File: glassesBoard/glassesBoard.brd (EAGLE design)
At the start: 82.9 x 28.4 mm, 90 parts, among them J1 BM10NB(0.8)-16DS-0.4V(51), J2 DF30FC-30DS-0.4V, J3 S2B-XH-A(LF)(SN), J7 105450-0101, U10 ATTINY20-MMH, U11 SN65LVDS822VQFN48, U12 NLAS2750, U13 NX3020NAK, U14 SSM3J338RSOT-23F, U15 NX3020NAK, U16 SSM3J338RSOT-23F, U17 NX3020NAK, U18 2.8, U19 TCR2EF15SOT-25, U2 TPS613222A, U20 MICROSD, U21 MCP73833, U3 1.8, U4 3.3, U5 SSM3J338RSOT-23F, U6 SSM3J338RSOT-23F, U7 SN65DSI83PBGA-N64, U8 IQS263BDFN10, U9 NX3020NAK

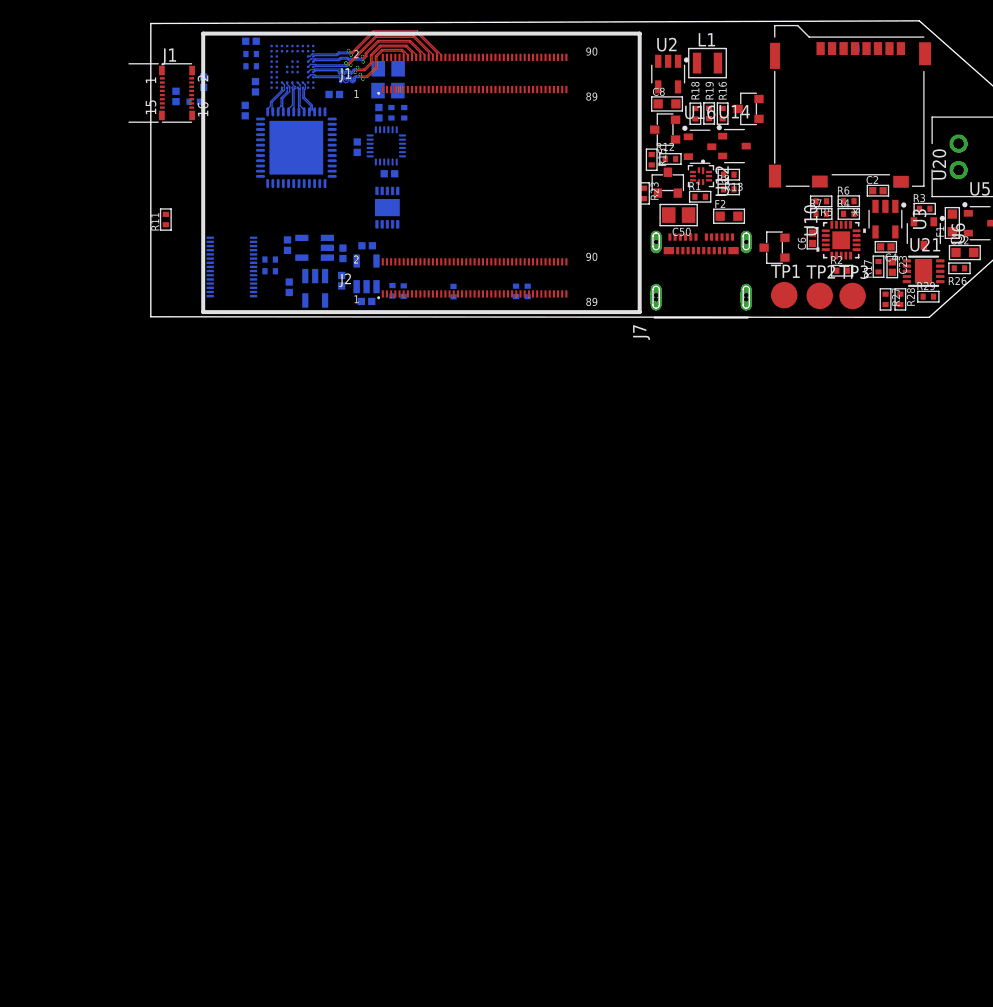
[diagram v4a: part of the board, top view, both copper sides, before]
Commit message: Added gesture board, more level shifting and light sensor
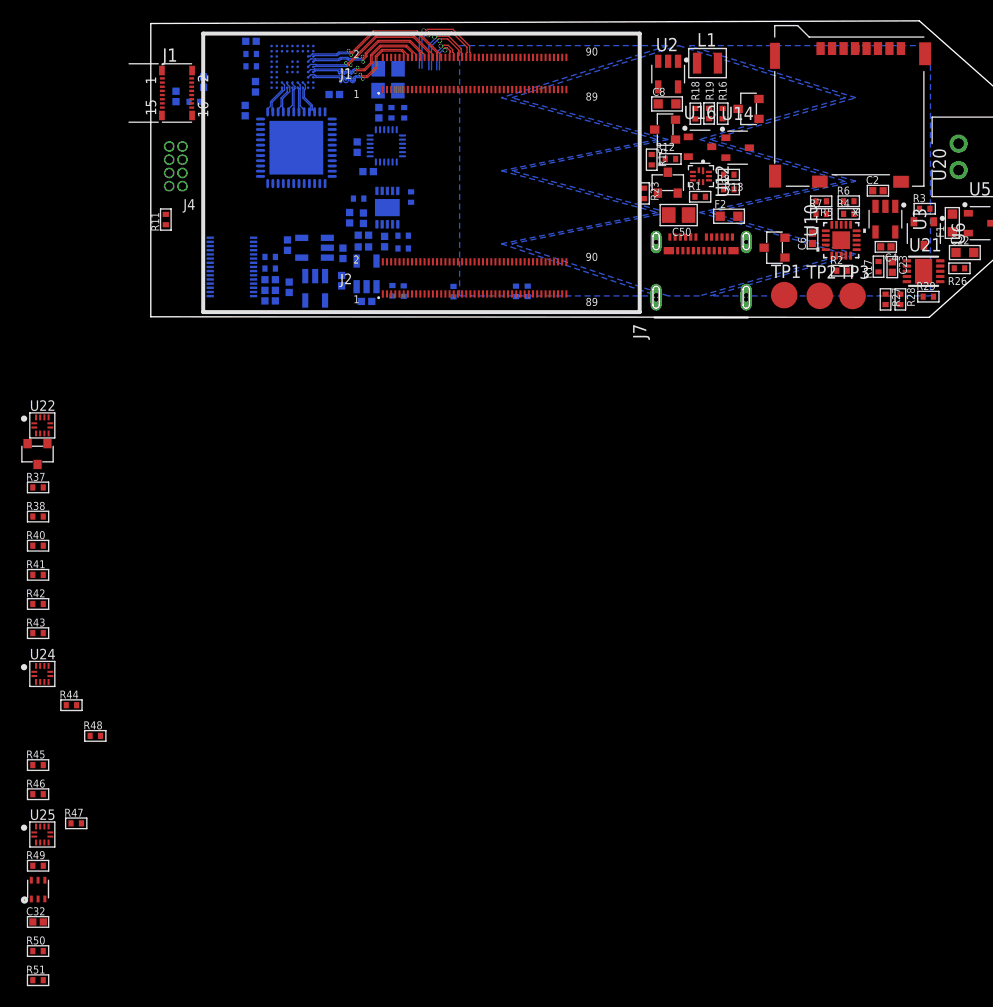
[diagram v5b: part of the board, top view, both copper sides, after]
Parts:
- added C25, C27, C29, C30, C31: 1uF, thanics-capacitor:C0402
- added C26, C28, C32: 100nF, thanics-capacitor:C0402
- added J4: GRPB042MWCN-RC, thanics-connector:GRPB042MWCN-RC
- added R34, R35, R36: 470R, thanics-resistor:R0402
- added R37, R41, R42, R43, R44, R45, R46, R47, R48, R49, R50, R51: 10k, thanics-resistor:R0402
- added R38, R39, R40: 5.1k, thanics-resistor:R0402
- added U22, U24, U25: FXMA2104UMX, glasses:12MLP
- added U23: NX3020NAK, glasses:SOT-23_(TO-236AB)
- added U26: LTR-303ALS-01, glasses:LTR-303ALS-01
- moved C20 2.06 mm to (25.1, 13.9), turned to 0 degrees
- moved C5 0.37 mm to (24.6, 6.71)
- moved U14 0.34 mm to (60.5, 16.2)
- moved R31 0.25 mm to (15.7, 5.74)
- moved R30 0.25 mm to (15.7, 4.62)
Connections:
- removed net !RST: R2.2, TP3.TP, U10.13
- removed net !SHUTDOWN_INT: U10.2
- removed net I2C_SCL_5V: U10.15
- removed net I2C_SDA_5V/TPIDATA: TP2.TP, U10.12
- new net !FINGER_INT_1V8: R48.1, U24.12
- new net !FINGER_INT_5V: R46.1, U10.14, U24.3
- new net !GESTURE_INT: R49.1, U$1.J2.52, U25.10
- new net !GESTURE_INT_3V3: J4.7, U25.5
- new net !LIGHT_INT: R50.1, U$1.J2.54, U25.9
- new net !LIGHT_INT_3V3: R51.1, U25.6, U26.5
- new net !SHUTDOWN_INT_1V8: R43.1, U22.9
- new net !SHUTDOWN_INT_5V: R41.1, U10.2, U22.6
- new net !TOUCH_INT_1V8: U24.11
- new net !TOUCH_INT_5V: R45.1, U10.17, U24.4
- new net !TPI_RST_1V8: R42.1, U22.12
- new net !TPI_RST_5V: R2.2, TP3.TP, U10.13, U22.3
- new net EXT_PROG_EN: U$1.J2.14, U23.G
- new net I2C0_SCL_3V3: J4.2, U25.4, U26.4
- new net I2C0_SCL_5V: R40.1, U10.15, U22.4
- new net I2C0_SDA_3V3: J4.8, U25.3, U26.6
- new net I2C0_SDA_5V/TPIDATA: R38.1, TP2.TP, U10.12, U22.5
- new net LED_B: J4.4, U$1.J2.60
- new net LED_G: J4.3, U$1.J2.58
- new net LED_R: J4.5, U$1.J2.6
- new net N$30: R36.1, U8.9
- new net N$31: R35.1, U8.3
- new net N$32: R34.1, U8.2
- new net N$33: R37.1, U22.8, U23.D
- new net N$35: R44.1, U24.8
- new net N$36: R47.1, U25.8
- new net N$37: C27.1, C28.1, U8.5
- new net RX1: R34.2
- new net RX2: R35.2
- new net RX3: R36.2
- net !TOUCH_INT: now also R39.1, U$1.J2.12
- net +1V5: now also C30.1
- net +1V8: now also C25.1, C26.1, C29.1, R39.2, R42.2, R43.2, R48.2, R49.2, R50.2, U11.17, U11.43, U11.6, U22.1, U24.1, U25.1, U8.4
- net +2V8: now also C31.1
- net +3V3: now also C32.1, J4.1, R47.2, R51.2, U25.2, U26.1; no longer U8.4
- net +5V: now also R37.2, R38.2, R40.2, R41.2, R44.2, R45.2, R46.2, U22.2, U24.2
- net DSI_EN: now also U$1.J2.63
- net GND: now also C25.2, C26.2, C27.2, C28.2, C29.2, C30.2, C31.2, C32.2, J4.6, U22.7, U23.S, U24.7, U25.7, U26.3, U8.1, U8.EXP
- net I2C0_SCL: now also U22.11, U25.11, U8.8
- net I2C0_SDA: now also U22.10, U25.12, U8.7
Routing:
- net MIPI_CSI1_DATA0_P: track 0.00 -> 10.2 mm, vias 0 -> 1
- net MIPI_CSI1_DATA0_N: track 0.00 -> 9.37 mm, vias 0 -> 1
- net MIPI_CSI1_DATA1_P: track 0.00 -> 7.53 mm, vias 0 -> 1
- net MIPI_CSI1_DATA1_N: track 0.00 -> 6.75 mm, vias 0 -> 1
- net MIPI_CSI1_CLK_P: track 0.00 -> 4.77 mm, vias 0 -> 1
- net MIPI_CSI1_CLK_N: track 0.00 -> 3.91 mm, vias 0 -> 1
- added copper zone on layer 16, net RX1
- added copper zone on layer 16, net RX2
- added copper zone on layer 16, net RX3

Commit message: Layout almost done
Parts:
- removed C16, C17, C21, C24: 1uF, thanics-capacitor:C0402
- removed R14, R25: 10k, thanics-resistor:R0402
- removed U11: SN65LVDS822VQFN48, glasses:QFN50P700X700X100-49T515
- removed U7: SN65DSI83PBGA-N64, glasses:BGA81C50P9X9_500X500X100
- added J10, J11, J5, J6, J8, J9: U.FL, thanics-connector:U.FL
- added R52: 10k, thanics-resistor:R0402
- moved R46 95.1 mm to (70.0, 10.7), turned to 90 degrees
- moved R45 92.4 mm to (68.6, 10.7), turned to 90 degrees
- moved R44 85.2 mm to (66.3, 11.8)
- moved U24 85.1 mm to (66.6, 9.86), turned to 90 degrees
- moved R41 82.6 mm to (69.2, 8.13)
- moved R48 81.8 mm to (64.1, 9.19), turned to 180 degrees
- moved R40 80.4 mm to (68.9, 5.69)
- moved R43 80.2 mm to (63.9, 7.95), turned to 180 degrees
- moved R38 80.1 mm to (69.2, 6.91)
- moved R42 77.9 mm to (63.8, 6.05), turned to 180 degrees
- moved R37 76.9 mm to (66.4, 7.95)
- moved R50 76.4 mm to (11.8, 13.3), flipped to the bottom, turned to 90 degrees
- moved R51 74.4 mm to (10.3, 8.84), flipped to the bottom, turned to 180 degrees
- moved U22 74.1 mm to (66.1, 6.10), turned to 90 degrees
- moved U23 72.6 mm to (64.1, 2.97), turned to 180 degrees
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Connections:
- removed net !SHUTDOWN_LVDS: U11.37
- removed net FINGER_INT: J1.8, U$1.J1.73
- removed net N$1: U11.26, U7.C8
- removed net N$10: U11.33, U7.G9
- removed net N$11: U11.32, U7.F8
- removed net N$12: U11.31, U7.F9
- removed net N$15: C16.1, U7.J8
- removed net N$26: R14.2, U7.A1, U7.H2
- removed net N$3: U11.25, U7.C9
- removed net N$4: U11.28, U7.D8
- removed net N$5: U11.27, U7.D9
- removed net N$7: U11.30, U7.E8
- removed net N$8: U11.29, U7.E9
- removed net N$9: U11.34, U7.G8
- new net N$34: R52.1
- net !FINGER_INT_1V8: now also J1.8, U$1.J1.73
- net !TOUCH_INT: no longer U$1.J2.12
- net !TOUCH_INT_1V8: now also U$1.J2.12
- net !TOUCH_INT_5V: now also U10.1; no longer U10.17
- net !TPI_RST_1V8: now also U22.11; no longer U22.12
- net !TPI_RST_5V: now also U22.4; no longer U22.3
- net +1V8: now also R52.2; no longer C17.1, R25.1, U11.17, U11.43, U11.6, U7.A9, U7.B8, U7.D6, U7.E5, U7.E6, U7.F6, U7.J2
- net +3V3: no longer C24.1, U11.24, U11.44
- net BATT_CNTL: now also U10.17; no longer U10.1
- net DSI_EN: no longer C21.1, R25.2, U7.B1
- net GND: now also J10.P$1, J10.P$2, J11.P$1, J11.P$2, J5.P$1, J5.P$2, J6.P$1, J6.P$2, J8.P$1, J8.P$2, J9.P$1, J9.P$2; no longer C16.2, C17.2, C21.2, C24.2, R14.1, U11.36, U11.45, U11.49, U7.A2, U7.A8, U7.B9, U7.D5, U7.E4, U7.F4, U7.F5, U7.H9
- net I2C0_SCL: now also U22.12; no longer U22.11
- net I2C0_SCL_5V: now also U22.3; no longer U22.4
- net I2C3_SCL: no longer U7.H1
- net I2C3_SDA: no longer U7.J1
- net LED_B: now also U$1.J2.2
- net LED_G: now also U$1.J2.8
- net MIPI_DSI0_CLK_N: now also J11.P$3; no longer U7.J5
- net MIPI_DSI0_CLK_P: now also J10.P$3; no longer U7.H5
- net MIPI_DSI0_DATA0_N: now also J6.P$3; no longer U7.J3
- net MIPI_DSI0_DATA0_P: now also J5.P$3; no longer U7.H3
- net MIPI_DSI0_DATA1_N: now also J9.P$3; no longer U7.J4
- net MIPI_DSI0_DATA1_P: now also J8.P$3; no longer U7.H4
- net MIPI_DSI0_DATA2_N: no longer U7.J6
- net MIPI_DSI0_DATA2_P: no longer U7.H6
- net MIPI_DSI0_DATA3_N: no longer U7.J7
- net MIPI_DSI0_DATA3_P: no longer U7.H7
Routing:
- net P$1: track 0.00 -> 104.2 mm, vias 0 -> 3
- net I2C0_SCL: track 0.00 -> 70.1 mm, vias 0 -> 6
- net I2C0_SDA: track 0.00 -> 69.6 mm, vias 0 -> 6
- net CHARGER_VCC: track 0.00 -> 62.2 mm, vias 0 -> 3
- net CHARGE_STAT2: track 0.00 -> 57.3 mm, vias 0 -> 2
- net CHARGE_STAT1: track 0.00 -> 57.0 mm, vias 0 -> 2
- net +5V: track 0.00 -> 51.0 mm, vias 0 -> 7
- net USB_HS_ID: track 0.00 -> 48.4 mm, vias 0 -> 6
- net MIPI_CSI1_DATA0_N: track 9.37 -> 54.9 mm, vias 1 -> 3
- net MIPI_CSI1_DATA0_P: track 10.2 -> 55.4 mm, vias 1 -> 3
- net SPI0_MISO: track 0.00 -> 43.1 mm, vias 0 -> 2
- net MIPI_CSI1_CLK_N: track 3.91 -> 44.9 mm, vias 1 -> 3
- net MIPI_CSI1_CLK_P: track 4.77 -> 45.7 mm, vias 1 -> 3
- net SPI0_MOSI: track 0.00 -> 40.6 mm, vias 0 -> 2
- net !FINGER_RST: track 0.00 -> 39.5 mm, vias 0 -> 3
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- added copper zone on layer 2, net +1V8
- added copper zone on layer 1, net GND
- added copper zone on layer 15, net GND
- added copper zone on layer 16, net GND
- removed copper zone on layer 16, net RX1
- removed copper zone on layer 16, net RX2
- removed copper zone on layer 16, net RX3
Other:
- board size 82.9 x 28.4 mm -> 82.9 x 29.2 mm

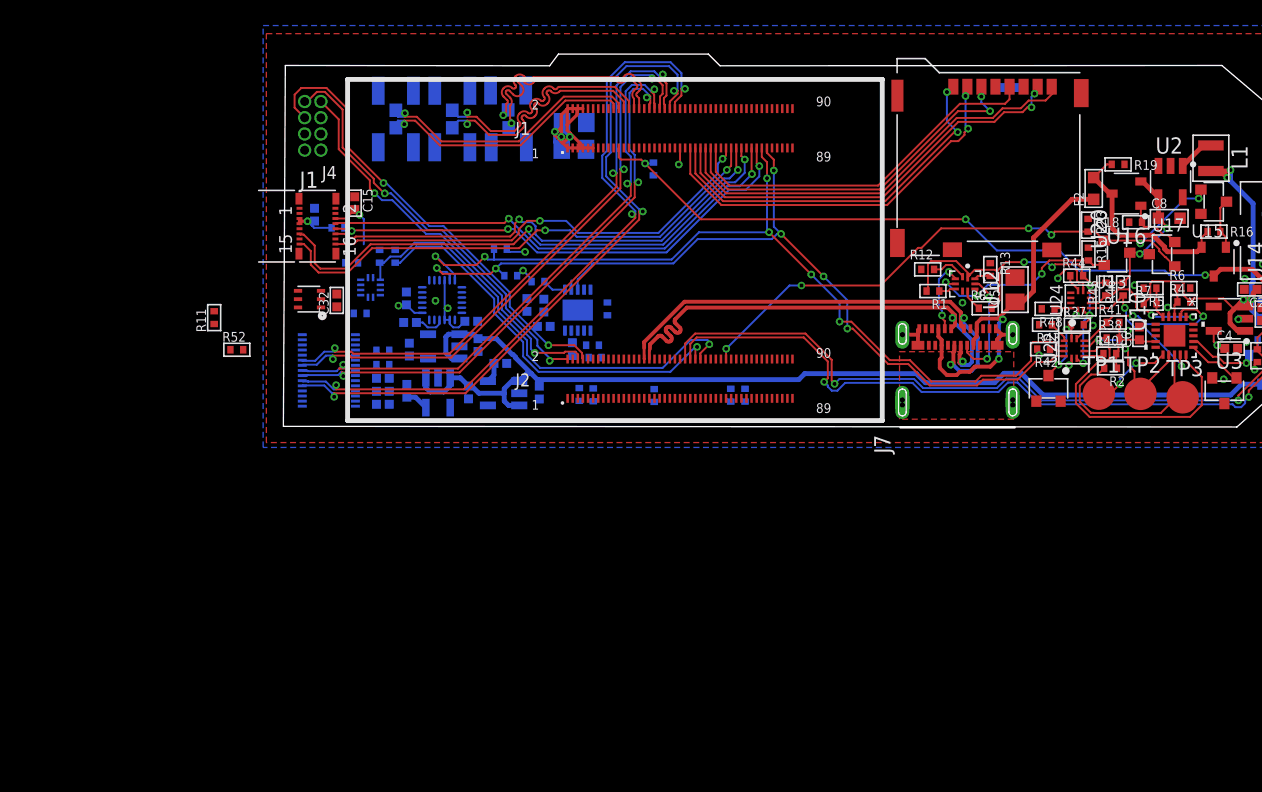
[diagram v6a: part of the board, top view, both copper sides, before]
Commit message: Removed light sensor, added serial port pins, added touch panel connector, small schematic fixes
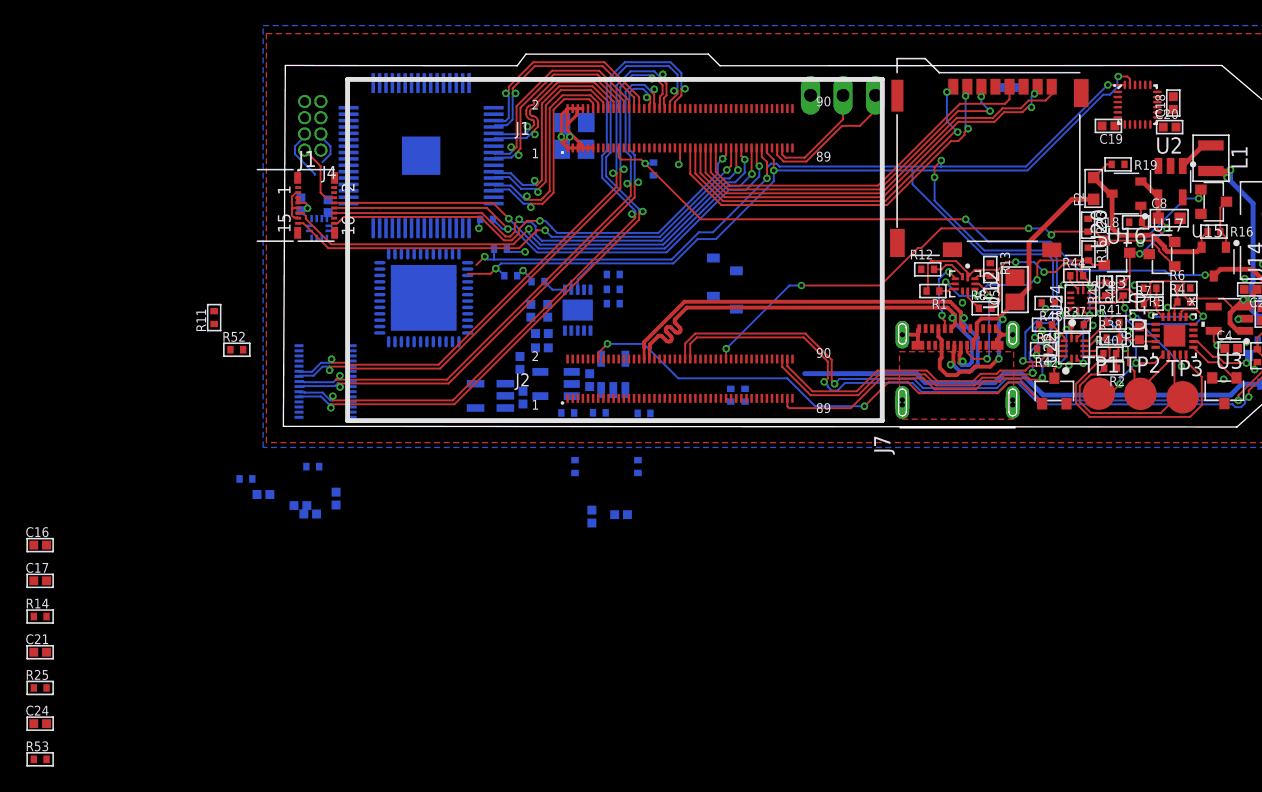
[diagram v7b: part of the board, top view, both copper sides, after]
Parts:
- removed C32: 100nF, thanics-capacitor:C0402
- removed J10, J11, J6, J8, J9: U.FL, thanics-connector:U.FL
- removed R50, R51: 10k, thanics-resistor:R0402
- removed U26: LTR-303ALS-01, glasses:LTR-303ALS-01
- added C16, C17, C21, C24: 1uF, thanics-capacitor:C0402
- added JP1: (no value), pinhead:1X03/90
- added R14, R25, R53: 10k, thanics-resistor:R0402
- added U11: SN65LVDS822VQFN48, glasses:QFN50P700X700X100-49T515
- added U7: SN65DSI83-Q1S-PQFP-G64, glasses:QFP50P1200X1200X120-65T300
- J5: value U.FL -> 0787324001; device thanics-connector:U.FL -> thanics-connector:0787324001
- moved C18 61.9 mm to (73.9, 25.3), flipped to the top
- moved C20 61.4 mm to (73.6, 23.4), flipped to the top
- moved U1 56.5 mm to (71.1, 25.2), flipped to the top
- moved C19 52.2 mm to (68.8, 23.5), flipped to the top
- moved R49 25.1 mm to (32.0, -3.15)
- moved R47 23.7 mm to (27.1, -3.15), turned to 90 degrees
- moved J5 22.7 mm to (38.8, 11.2), turned to 90 degrees
- moved C5 15.1 mm to (30.7, -6.91)
- moved R31 14.7 mm to (1.32, -4.11)
- moved C29 13.0 mm to (2.69, -5.33)
- moved R20 11.7 mm to (20.2, 16.2)
- moved C30 11.0 mm to (5.59, -6.20)
- moved C3 10.5 mm to (28.4, -7.06)
- moved C31 10.3 mm to (6.35, -6.86)
- moved C13 10.1 mm to (8.38, -5.65)
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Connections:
- removed net !LIGHT_INT: R50.1, U$1.J2.54, U25.9
- removed net !LIGHT_INT_3V3: R51.1, U25.6, U26.5
- new net !SHUTDOWN_LVDS: U11.37
- new net N$1: U11.26, U7.46
- new net N$10: U11.33, U7.37
- new net N$11: U11.32, U7.38
- new net N$12: U11.31, U7.39
- new net N$15: R53.2, U7.17
- new net N$26: C17.1, U7.31
- new net N$3: U11.25, U7.47
- new net N$39: R25.2, U7.64
- new net N$4: U11.28, U7.44
- new net N$5: U11.27, U7.45
- new net N$7: U11.30, U7.41
- new net N$8: U11.29, U7.42
- new net N$9: U11.34, U7.36
- new net TPICLK_1V8: U$1.J2.87, U24.12
- new net UART1_RX: JP1.2, U$1.J1.85
- new net UART1_TX: JP1.1, U$1.J1.83
- net !FINGER_INT_1V8: now also U24.11; no longer U24.12
- net !FINGER_INT_5V: now also U24.4; no longer U24.3
- net !SHUTDOWN_INT_1V8: now also U$1.J2.88
- net !TOUCH_INT_1V8: now also U24.10; no longer U24.11
- net !TOUCH_INT_5V: now also U24.5; no longer U24.4
- net !TPI_RST_1V8: now also U$1.J2.86
- net +1V8: now also C16.1, R14.1, U11.17, U11.43, U11.6, U7.14, U7.18, U7.3, U7.32, U7.35, U7.40, U7.43, U7.48, U7.49, U7.55, U7.58, U7.63; no longer R50.2
- net +3V3: now also C24.1, U11.24, U11.44; no longer C32.1, R51.2, U26.1
- net DSI_EN: now also C21.1, R14.2, U7.2
- net GND: now also C16.2, C17.2, C21.2, C24.2, J5.4, JP1.3, R25.1, R53.1, U11.36, U11.45, U11.49, U7.23, U7.26, U7.52, U7.65; no longer C32.2, J10.P$1, J10.P$2, J11.P$1, J11.P$2, J5.P$1, J5.P$2, J6.P$1, J6.P$2, J8.P$1, J8.P$2, J9.P$1, J9.P$2, U26.3
- net I2C0_SCL_3V3: no longer U26.4
- net I2C0_SDA_3V3: no longer U26.6
- net I2C3_SCL: now also U7.15
- net I2C3_SDA: now also U7.16
- net MIPI_DSI0_CLK_N: now also U7.25; no longer J11.P$3
- net MIPI_DSI0_CLK_P: now also U7.24; no longer J10.P$3
- net MIPI_DSI0_DATA0_N: now also U7.20; no longer J6.P$3
- net MIPI_DSI0_DATA0_P: now also U7.19; no longer J5.P$3
- net MIPI_DSI0_DATA1_N: now also U7.22; no longer J9.P$3
- net MIPI_DSI0_DATA1_P: now also U7.21; no longer J8.P$3
- net MIPI_DSI0_DATA2_N: now also U7.28
- net MIPI_DSI0_DATA2_P: now also U7.27
- net MIPI_DSI0_DATA3_N: now also U7.30
- net MIPI_DSI0_DATA3_P: now also U7.29
- net RX1: now also J5.2
- net RX2: now also J5.1
- net RX3: now also J5.3
- net TPICLK: now also U24.3
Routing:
- net P$1: track 104.2 -> 54.5 mm, vias 3 -> 2
- net EXT_PROG_EN: track 0.00 -> 39.7 mm, vias 0 -> 2
- net LED_G: track 36.3 -> 0.00 mm, vias 2 -> 0
- net !LIGHT_INT: track 35.8 -> 0.00 mm, vias 1 -> 0
- net LED_B: track 32.7 -> 0.00 mm, vias 2 -> 0
- net LED_R: track 31.6 -> 0.00 mm, vias 2 -> 0
- net !GESTURE_INT: track 31.3 -> 0.00 mm, vias 1 -> 0
- net TPICLK_1V8: track 0.00 -> 29.0 mm, vias 0 -> 2
- net !TPI_RST_1V8: track 1.18 -> 27.5 mm, vias 0 -> 3
- net !SHUTDOWN_INT_1V8: track 1.65 -> 27.8 mm, vias 0 -> 2
- net I2C0_SCL: track 70.1 -> 92.5 mm, vias 6 -> 4
- net MIPI_DSI0_DATA2_P: track 0.00 -> 17.9 mm, vias 0 -> 1
- net I2C0_SDA: track 69.6 -> 86.9 mm
- net MIPI_DSI0_DATA3_P: track 0.00 -> 17.1 mm, vias 0 -> 1
- net MIPI_DSI0_DATA2_N: track 0.00 -> 17.0 mm, vias 0 -> 1
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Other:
- outline, holes or cut-outs redrawn
- board text added: "G"
- board text added: "RX"
- board text added: "TX"
